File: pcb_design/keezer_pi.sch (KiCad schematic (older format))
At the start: 10 parts, among them Q1 PN2222A, T1 CONN_01X03_FEMALE, T2 CONN_01X03_FEMALE, T3 CONN_01X03_FEMALE

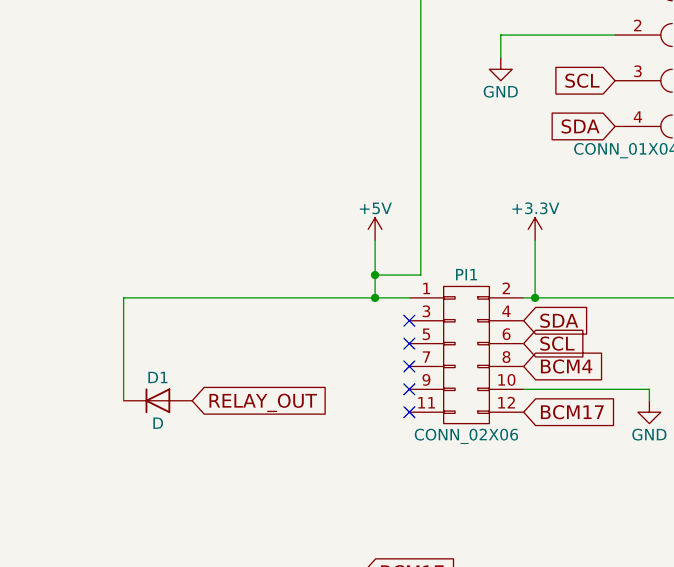
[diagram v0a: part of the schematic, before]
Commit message: Update pcb file names, remove duplicate files
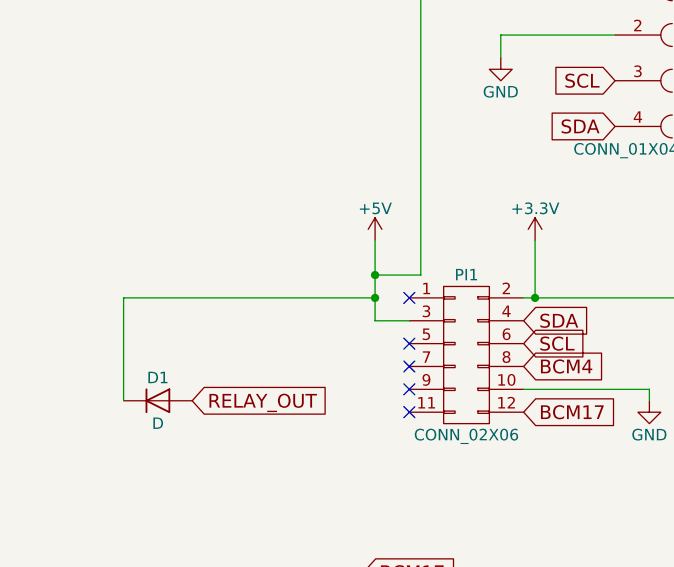
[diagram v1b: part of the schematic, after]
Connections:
- net +5V: now also PI1.3 (P3); no longer PI1.1 (P1)
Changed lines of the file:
@@
 LIBS:valves
 LIBS:pi_zero
-LIBS:keezer-cache
+LIBS:keezer_pi-cache
 EELAYER 25 0
 EELAYER END
@@
 Text GLabel 5050 5050 2    60   Input ~ 0
 TRANSISTOR_BASE
-NoConn ~ 5250 3650
 NoConn ~ 5250 3850
 NoConn ~ 5250 3950
@@
 	5800 3300 5800 3550
 Wire Wire Line
-	4000 3550 5250 3550
-Wire Wire Line
-	5100 3550 5100 3300
+	5100 3300 5100 3650
 Wire Wire Line
 	5750 3950 6300 3950
@@
 Wire Wire Line
 	7400 4050 7100 4050
+NoConn ~ 5250 3550
+Wire Wire Line
+	5100 3650 5250 3650
+Wire Wire Line
+	4000 3550 5100 3550
 $EndSCHEMATC
